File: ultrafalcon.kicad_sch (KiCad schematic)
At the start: 44 parts, among them J1 Conn_01x08_Socket, SW1 PER601-P117-N0015, SW2 SW_Push, U1 SK6805-EC15, U10 SK6805-EC15, U11 SK6805-EC15, U12 SK6805-EC15, U13 SK6805-EC15, U14 SK6805-EC15, U15 SK6805-EC15, U16 SK6805-EC15, U17 SK6805-EC15, U18 SK6805-EC15, U19 SK6805-EC15, U2 SK6805-EC15, U20 SK6805-EC15, U21 SK6805-EC15, U22 SK6805-EC15, U23 SK6805-EC15, U24 SK6805-EC15, U25 SK6805-EC15, U26 SK6805-EC15, U27 SK6805-EC15, U28 SK6805-EC15, U29 SK6805-EC15, U3 SK6805-EC15, U30 SK6805-EC15, U4 SK6805-EC15, U5 SK6805-EC15, U6 SK6805-EC15, U7 SK6805-EC15, U8 SK6805-EC15, U9 SK6805-EC15

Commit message: jan22 updates, almost ready for production
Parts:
- added J2: Conn_01x02_Socket, Connector_PinHeader_2.54mm:PinHeader_1x02_P2.54mm_Vertical, symbol Connector:Conn_01x02_Socket
- added LOGO2: **REF, ct-kicad:pcbway-logo-neg40mm, symbol ct-kicad:pcbway-logo
- added LOGO3: **REF, ct-kicad:ultrafalcon-qr, symbol ct-kicad:ultrafalcon-qr
- C3: value 100uF -> 1uF
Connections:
- net SWITCH_A: now also J2.1 (Pin_1)
- net SWITCH_B: now also J2.2 (Pin_2)
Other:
- moved on the sheet: SW2
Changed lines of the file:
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@@
   (junction (at 198.12 135.89) (diameter 0) (color 0 0 0 0)
   )
-  (no_connect (at 262.89 92.71))
-  (no_connect (at 278.13 92.71))
+  (no_connect (at 276.86 93.98))
+  (no_connect (at 292.1 93.98))
   (wire (pts (xy 148.59 69.85) (xy 152.4 69.85))
     (stroke (width 0) (type default))
@@
     (stroke (width 0) (type default))
   )
-  (wire (pts (xy 262.89 92.71) (xy 265.43 92.71))
+  (wire (pts (xy 276.86 93.98) (xy 279.4 93.98))
     (stroke (width 0) (type default))
   )
@@
     (stroke (width 0) (type default))
   )
-  (wire (pts (xy 275.59 92.71) (xy 278.13 92.71))
+  (wire (pts (xy 289.56 93.98) (xy 292.1 93.98))
     (stroke (width 0) (type default))
   )
@@
     (stroke (width 0) (type default))
   )
+  (wire (pts (xy 287.02 105.41) (xy 290.83 105.41))
+    (stroke (width 0) (type default))
+  )
   (wire (pts (xy 198.12 135.89) (xy 198.12 137.16))
     (stroke (width 0) (type default))
@@
     (stroke (width 0) (type default))
   )
+  (wire (pts (xy 287.02 107.95) (xy 290.83 107.95))
+    (stroke (width 0) (type default))
+  )
   (wire (pts (xy 116.84 232.41) (xy 116.84 233.68))
     (stroke (width 0) (type default))
@@
   )
   (text_box "1uF capacitor for LEDs"
-    (at 193.04 91.44 0) (size 24.13 8.89)
+    (at 191.77 96.52 0) (size 25.4 3.81)
     (stroke (width 0) (type default))
     (fill (type none))
@@
   )
   (text_box "MX switch will be bodge wired for simplicity to pins7/8 of JST socket."
-    (at 257.81 73.66 0) (size 26.67 10.16)
+    (at 271.78 74.93 0) (size 26.67 10.16)
+    (stroke (width 0) (type default))
+    (fill (type none))
+    (effects (font (size 1.27 1.27)) (justify left top))
+  )
+  (text_box "Why does this chain seem to run from front to back, you ask?\n\nWell, I changed footprints and I'm inexperienced.  So there you go."
+    (at 208.28 217.17 0) (size 38.1 15.24)
     (stroke (width 0) (type default))
     (fill (type none))
@@
     (effects (font (size 1.27 1.27)) (justify left top))
   )
+  (text_box "JST-XH 2.54"
+    (at 226.06 81.28 0) (size 15.24 3.81)
+    (stroke (width 0) (type default))
+    (fill (type none))
+    (effects (font (size 1.27 1.27)) (justify left top))
+  )
   (global_label "LED_DI" (shape output) (at 243.84 99.06 0) (fields_autoplaced)
     (effects (font (size 1.27 1.27)) (justify left))
@@
     )
   )
+  (global_label "SWITCH_A" (shape input) (at 290.83 107.95 0) (fields_autoplaced)
+    (effects (font (size 1.27 1.27)) (justify left))
+    (property "Intersheetrefs" "${INTERSHEET_REFS}" (at 302.7052 107.95 0)
+      (effects (font (size 1.27 1.27)) (justify left) hide)
+    )
+  )
   (global_label "ENCODER_B" (shape input) (at 135.89 105.41 180) (fields_autoplaced)
     (effects (font (size 1.27 1.27)) (justify right))
@@
     )
   )
+  (global_label "SWITCH_B" (shape output) (at 290.83 105.41 0) (fields_autoplaced)
+    (effects (font (size 1.27 1.27)) (justify left))
+    (property "Intersheetrefs" "${INTERSHEET_REFS}" (at 302.8866 105.41 0)
+      (effects (font (size 1.27 1.27)) (justify left) hide)
+    )
+  )
   (global_label "ENCODER_A" (shape input) (at 243.84 104.14 0) (fields_autoplaced)
     (effects (font (size 1.27 1.27)) (justify left))
@@
     )
   )
-  (symbol (lib_id "Switch:SW_Push") (at 270.51 92.71 0) (unit 1)
+  (symbol (lib_id "Switch:SW_Push") (at 284.48 93.98 0) (unit 1)
     (in_bom no) (on_board yes) (dnp no) (fields_autoplaced)
-    (property "Reference" "SW2" (at 270.51 85.09 0)
+    (property "Reference" "SW2" (at 284.48 86.36 0)
       (effects (font (size 1.27 1.27)))
     )
-    (property "Value" "SW_Push" (at 270.51 87.63 0)
+    (property "Value" "SW_Push" (at 284.48 88.9 0)
       (effects (font (size 1.27 1.27)))
     )
-    (property "Footprint" "ct-kicad:SW_MX_cutout" (at 270.51 87.63 0)
+    (property "Footprint" "ct-kicad:SW_MX_cutout" (at 284.48 88.9 0)
       (effects (font (size 1.27 1.27)) hide)
     )
-    (property "Datasheet" "~" (at 270.51 87.63 0)
+    (property "Datasheet" "~" (at 284.48 88.9 0)
       (effects (font (size 1.27 1.27)) hide)
     )
@@
       (effects (font (size 1.27 1.27)))
     )
-    (property "Value" "100uF" (at 204.47 105.41 0)
+    (property "Value" "1uF" (at 204.47 105.41 0)
       (effects (font (size 1.27 1.27)))
     )
@@
     )
   )
+  (symbol (lib_id "Connector:Conn_01x02_Socket") (at 281.94 107.95 180) (unit 1)
+    (in_bom yes) (on_board yes) (dnp no) (fields_autoplaced)
+    (property "Reference" "J2" (at 282.575 100.33 0)
+      (effects (font (size 1.27 1.27)))
+    )
+    (property "Value" "Conn_01x02_Socket" (at 282.575 102.87 0)
+      (effects (font (size 1.27 1.27)))
+    )
+    (property "Footprint" "Connector_PinHeader_2.54mm:PinHeader_1x02_P2.54mm_Vertical" (at 281.94 107.95 0)
+      (effects (font (size 1.27 1.27)) hide)
+    )
+    (property "Datasheet" "~" (at 281.94 107.95 0)
+      (effects (font (size 1.27 1.27)) hide)
+    )
+    (pin "2")
+    (pin "1")
+    (instances
+      (project "ultrafalcon"
+        (path "/7e990e0f-d17d-4d94-84c9-ab822ccf2d6e"
+          (reference "J2") (unit 1)
+        )
+      )
+    )
+  )
   (symbol (lib_id "ct-kicad:SK6805-EC15") (at 198.12 177.8 180) (unit 1)
     (in_bom yes) (on_board yes) (dnp no)
@@
     )
   )
+  (symbol (lib_id "ct-kicad:pcbway-logo") (at 41.91 104.14 0) (unit 1)
+    (in_bom no) (on_board yes) (dnp no) (fields_autoplaced)
+    (property "Reference" "LOGO2" (at 44.45 102.87 0)
+      (effects (font (size 1.27 1.27)) (justify left))
+    )
+    (property "Value" "**REF" (at 44.45 105.41 0)
+      (effects (font (size 1.27 1.27)) (justify left))
+    )
+    (property "Footprint" "ct-kicad:pcbway-logo-neg40mm" (at 41.91 104.14 0)
+      (effects (font (size 1.27 1.27)) hide)
+    )
+    (property "Datasheet" "" (at 41.91 104.14 0)
+      (effects (font (size 1.27 1.27)) hide)
+    )
+    (instances
+      (project "ultrafalcon"
+        (path "/7e990e0f-d17d-4d94-84c9-ab822ccf2d6e"
+          (reference "LOGO2") (unit 1)
+        )
+      )
+    )
+  )
   (symbol (lib_id "power:VCC") (at 104.14 152.4 180) (unit 1)
     (in_bom yes) (on_board yes) (dnp no) (fields_autoplaced)
@@
         )
       )
+    )
+  )
+  (symbol (lib_id "ct-kicad:ultrafalcon-qr") (at 57.15 96.52 0) (unit 1)
+    (in_bom no) (on_board yes) (dnp no) (fields_autoplaced)
+    (property "Reference" "LOGO3" (at 59.69 95.25 0)
+      (effects (font (size 1.27 1.27)) (justify left))
+    )
+    (property "Value" "**REF" (at 59.69 97.79 0)
+      (effects (font (size 1.27 1.27)) (justify left))
+    )
+    (property "Footprint" "ct-kicad:ultrafalcon-qr" (at 57.15 96.52 0)
+      (effects (font (size 1.27 1.27)) hide)
+    )
+    (property "Datasheet" "" (at 57.15 96.52 0)
+      (effects (font (size 1.27 1.27)) hide)
+    )
+    (instances
+      (project "ultrafalcon"
+        (path "/7e990e0f-d17d-4d94-84c9-ab822ccf2d6e"
+          (reference "LOGO3") (unit 1)
+        )
+      )

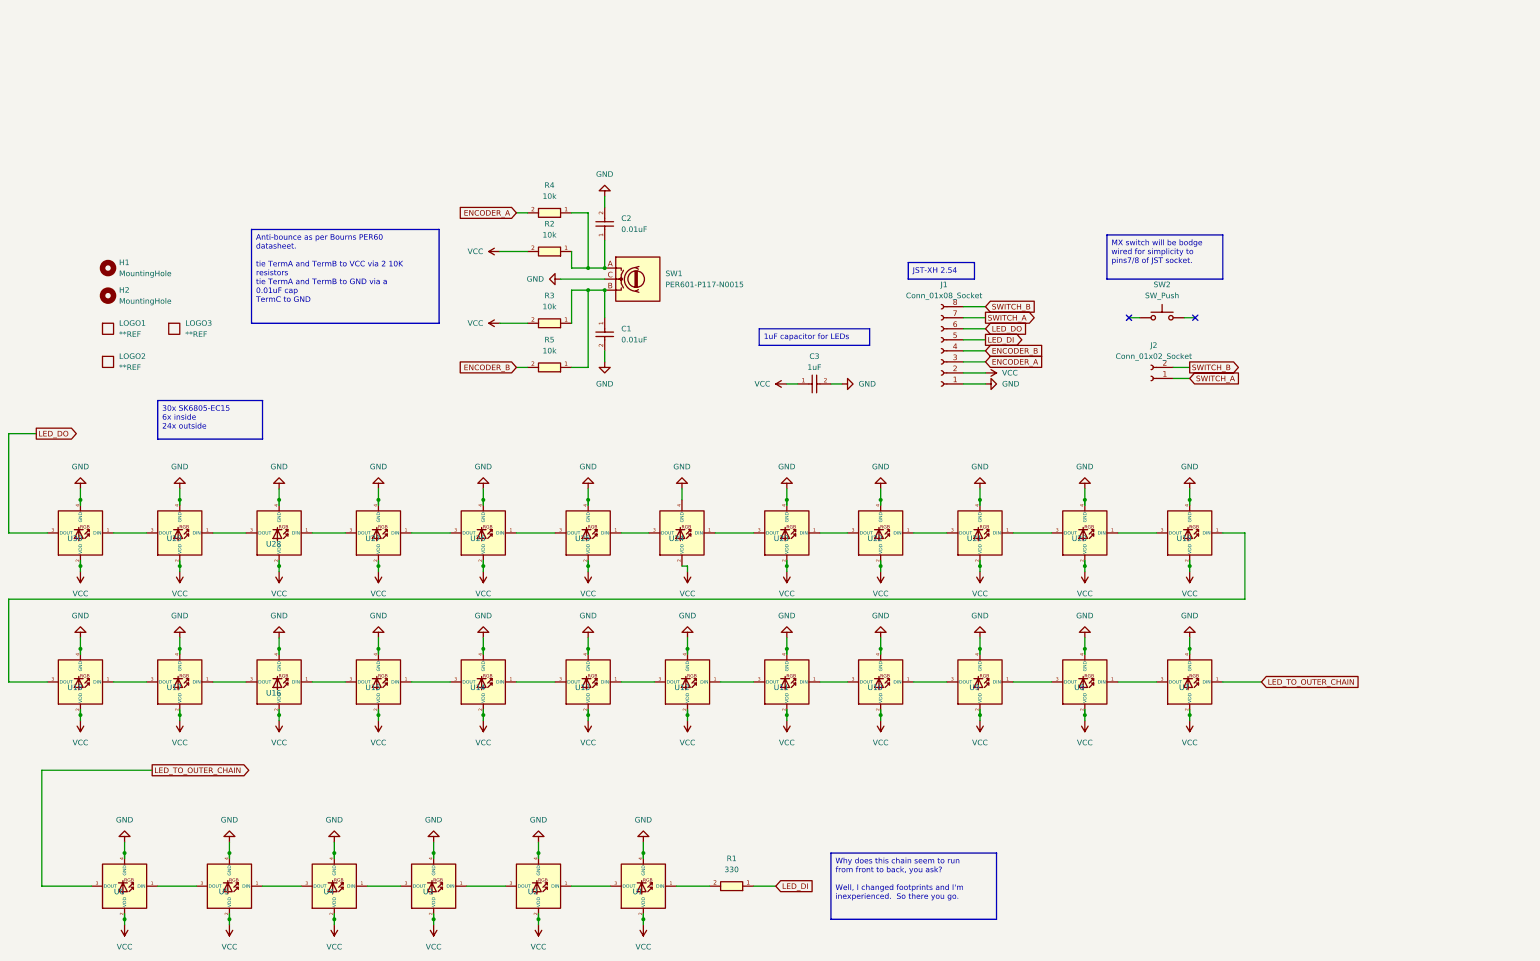
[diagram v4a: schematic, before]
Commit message: updating the pictures and schematic to match new pins
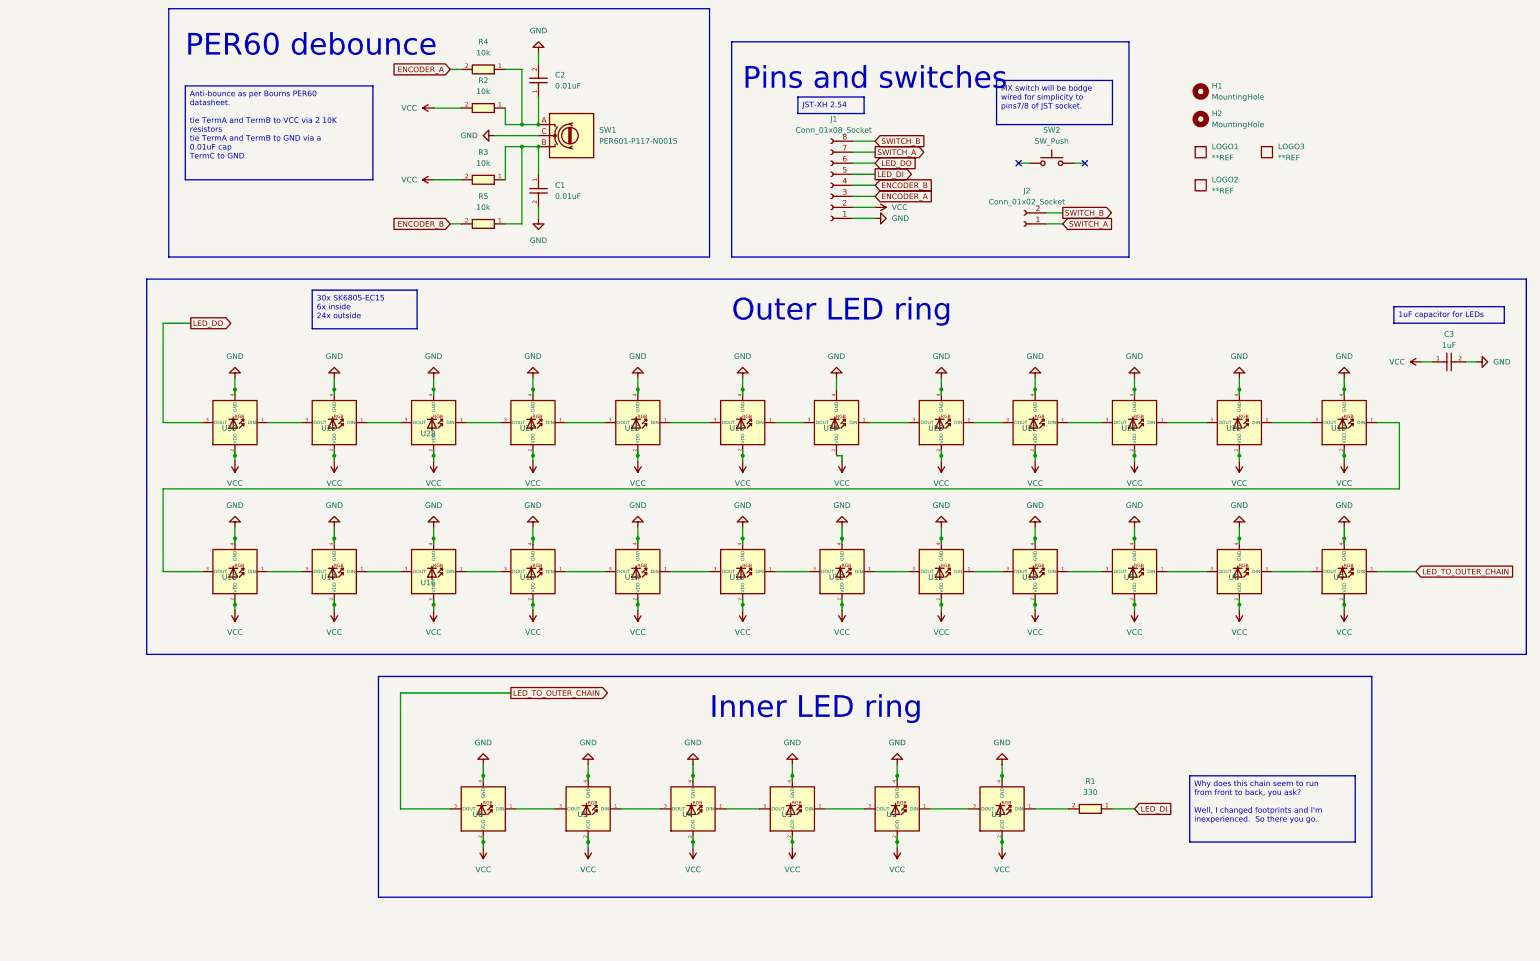
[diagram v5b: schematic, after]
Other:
- note added: "Inner LED ring"
- note added: "Outer LED ring"
- note added: "PER60 debounce"
- note added: "Pins and switches"
- company: (none) -> Author: Crazymittens
- title: (none) -> Ultrafalcon
- moved on the sheet: C1, C2, C3, H1, H2, J1, J2, LOGO1, LOGO2, LOGO3, R1, R2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

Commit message: final changes before submitting
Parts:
- J2: now left out of the parts list
- LOGO3: footprint ct-kicad:ultrafalcon-qr -> ct-kicad:ultrafalcon-qr-15mm
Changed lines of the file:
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@@
   )
   (symbol (lib_id "Connector:Conn_01x02_Socket") (at 252.73 72.39 180) (unit 1)
-    (in_bom yes) (on_board yes) (dnp no) (fields_autoplaced)
+    (in_bom no) (on_board yes) (dnp no) (fields_autoplaced)
     (property "Reference" "J2" (at 253.365 64.77 0)
       (effects (font (size 1.27 1.27)))
@@
       (effects (font (size 1.27 1.27)) (justify left))
     )
-    (property "Footprint" "ct-kicad:ultrafalcon-qr" (at 308.61 55.88 0)
-      (effects (font (size 1.27 1.27)) hide)
-    )
+    (property "Footprint" "ct-kicad:ultrafalcon-qr-15mm" (at 308.61 55.88 0)
+      (effects (font (size 1.27 1.27)) hide)
+    )

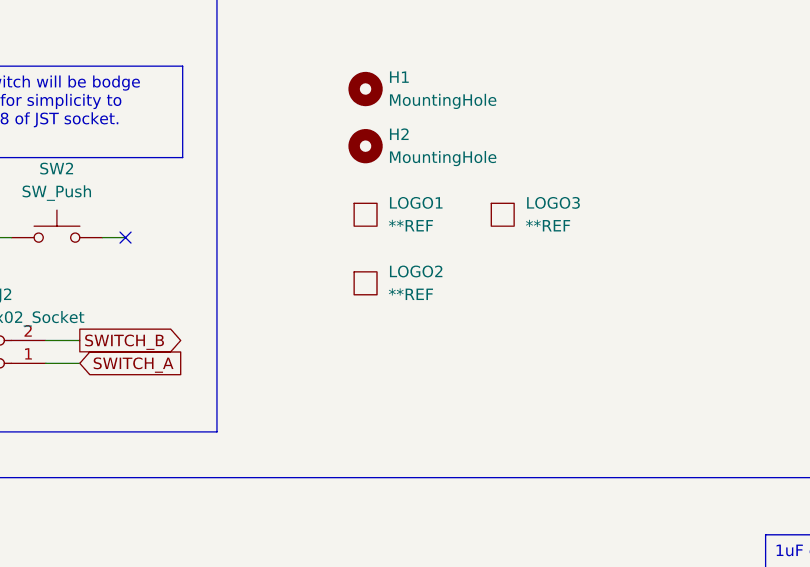
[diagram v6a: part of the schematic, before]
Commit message: fixed the incorrect footprint silkscreen
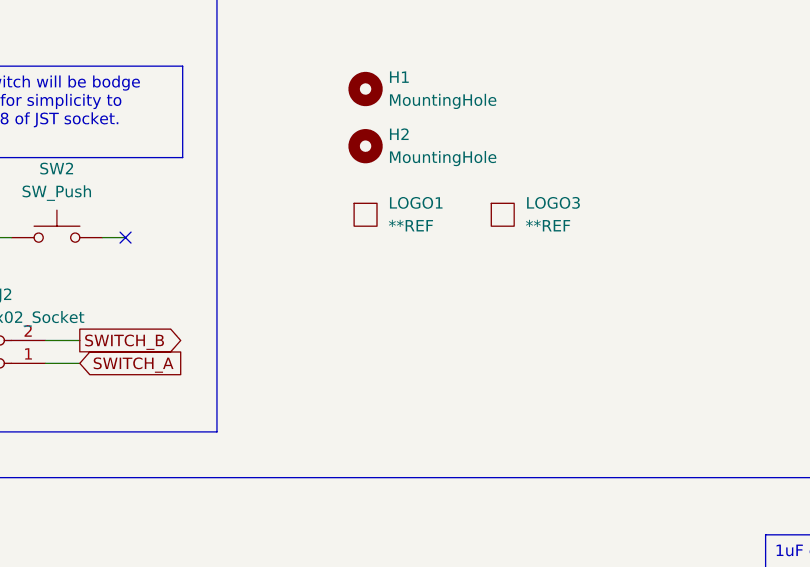
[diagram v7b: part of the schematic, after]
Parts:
- removed LOGO2: **REF, ct-kicad:pcbway-logo-neg40mm, symbol ct-kicad:pcbway-logo
- SW1: now left out of the parts list
